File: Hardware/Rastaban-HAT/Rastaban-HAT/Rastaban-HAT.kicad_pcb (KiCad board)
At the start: 2 copper layers, 99.1 x 99.7 mm, 129 parts, among them IC1 BCR420UW6-7, IC2 BCM53DS, J1 1778780, J10 GPIO, J11 Conn_01x06_Male, J12 Conn_01x03_Male, J13 Conn_01x03_Male, J2 1778780, J3 1778780, J4 Screw_Terminal_01x02, J5 Jack-DC 12V+, J6 SM04B-SRSS-TB(LF)(SN), J7 Screw_Terminal_01x02, J8 Screw_Terminal_01x02, J9 Conn_01x05_Male, M1 Fan, Q1 PMV15ENE, Q2 PMV15ENE, Q3 DMG2305UX-7, Q4 PMV15ENE, Q5 PMV15ENE, Q6 2N70002HWX, U1 DRV8870DDA, U10 xl6009_module, U2 TLV1117-33, U3 TMC2208_Carrier, U4 TMC2208_Carrier, U5 RT7272AGSP, U6 TMC2208_Carrier, U7 DRV8838 POLOLU, U8 TLV1117-33, U9 CAT24C256

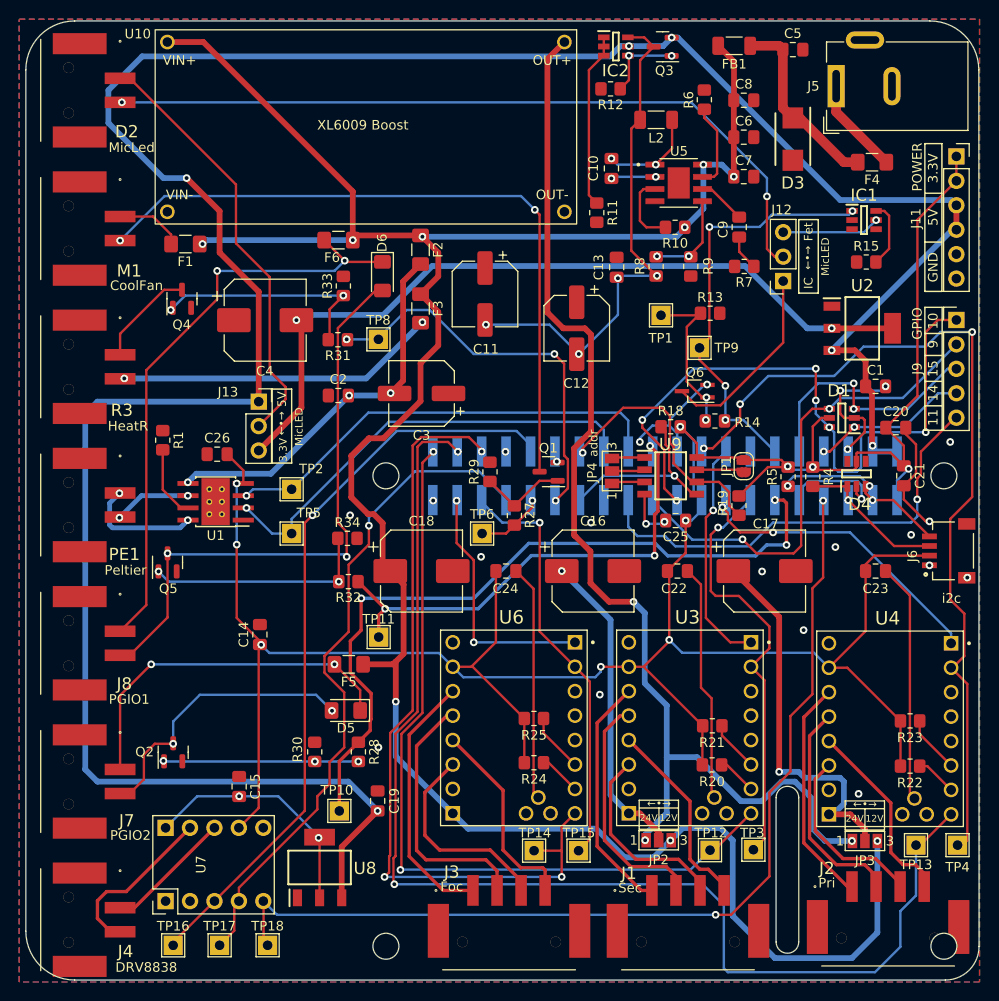
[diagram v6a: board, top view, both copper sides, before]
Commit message: created rounded tracks design
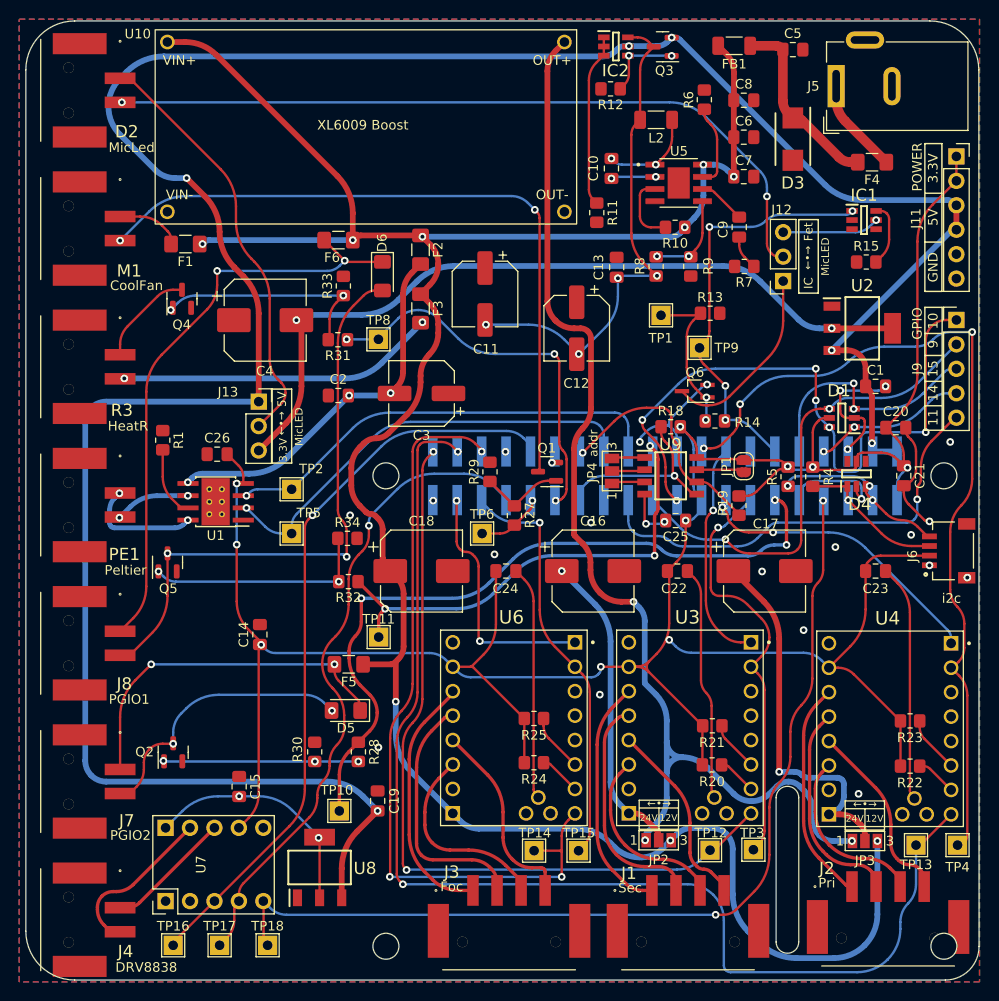
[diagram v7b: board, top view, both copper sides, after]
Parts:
- moved Q1 0.16 mm to (206.8, 158.0)
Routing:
- net 12V+: track 251.4 -> 245.7 mm
- net 5V+: track 272.5 -> 268.9 mm
- net ENSEC: track 128.7 -> 126.2 mm
- net PHADRV: track 70.2 -> 67.7 mm
- net 3.3V+: track 282.8 -> 280.6 mm
- net STEPSEC: track 90.8 -> 88.9 mm
- net ENFOC: track 82.8 -> 81.3 mm
- net ID_SCL: track 26.6 -> 25.1 mm
- net SLEEP: track 101.1 -> 99.7 mm
- net PWRGPIO1: track 78.1 -> 76.7 mm
- net Net-(C4-Pad2): track 82.6 -> 81.3 mm
- net ENPRI: track 83.8 -> 82.5 mm
- net GPIO10: track 68.6 -> 67.5 mm
- net Net-(D2-PadA): track 45.0 -> 43.9 mm
- net /FluidMotors/OA2PRI: track 20.3 -> 19.2 mm
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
